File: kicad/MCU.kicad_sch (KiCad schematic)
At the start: 77 parts, among them J3 USART, J4 FAN, J5 USB_A, J6 Display, Q7 2N7002NXAK, Q8 2N7002K, Q9 2N7002K, SW1 ENC0 (Voltage), SW2 ENC1 (Current), SW3 BOOT, SW4 RST, U6 USBLC6-2SC6, U7 MCP9700A, U8 STM32F373C8Tx, Y1 Crystal

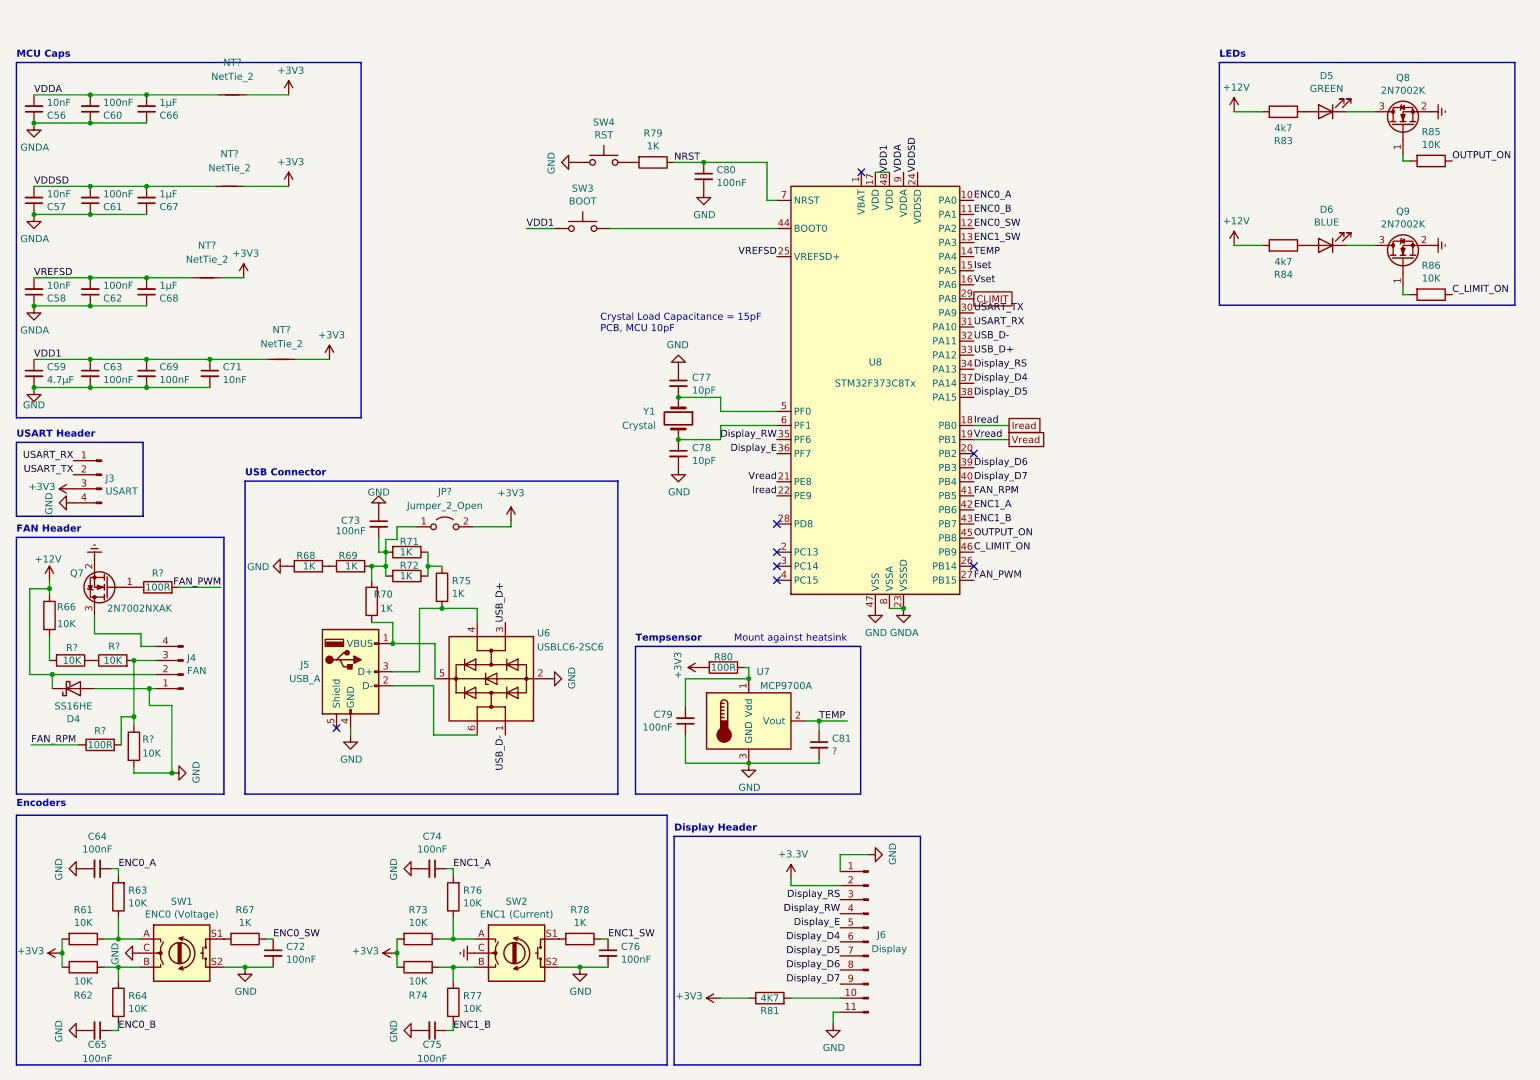
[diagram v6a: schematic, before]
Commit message: Updated files to kicad 8
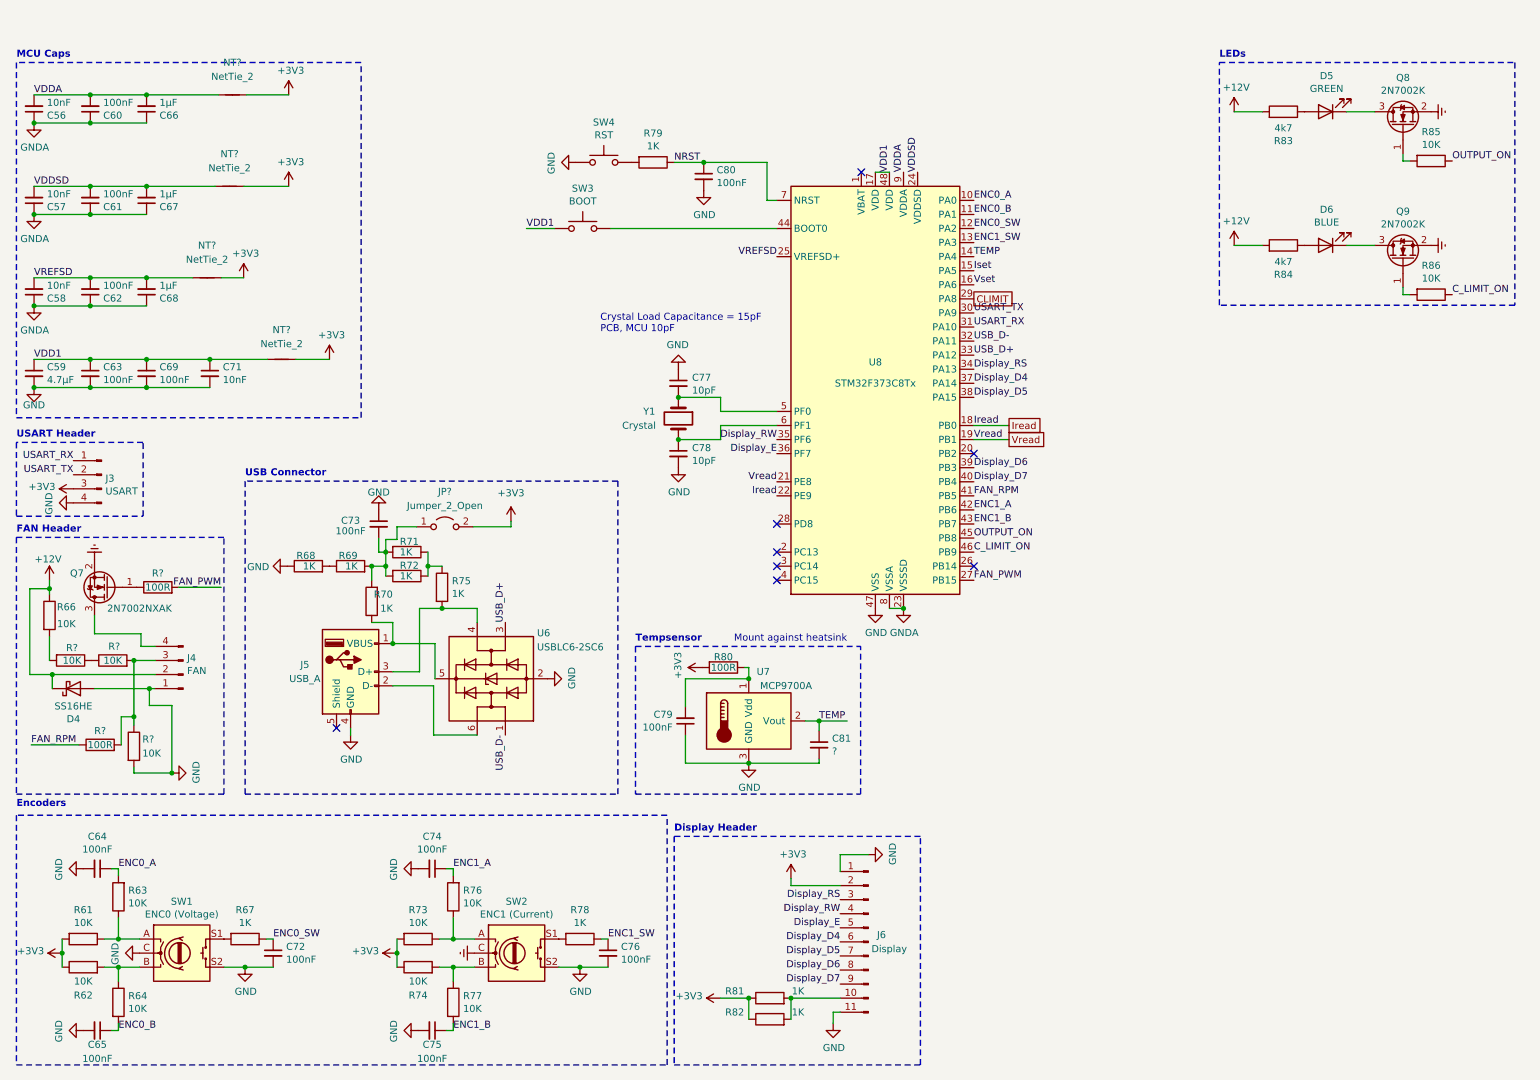
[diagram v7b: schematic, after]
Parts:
- added R82: 1K, Resistor_SMD:R_0805_2012Metric_Pad1.15x1.40mm_HandSolder, symbol Device:R
- R81: value 4K7 -> 1K
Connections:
- net +3V3: now also R82.1
- net at J6.10 (Pin_10), R81.2: now also R82.2

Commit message: Fixed a bunch of alignment
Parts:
- removed U8: STM32F373C8Tx, Package_QFP:LQFP-48_7x7mm_P0.5mm, symbol MCU_ST_STM32F3:STM32F373C8Tx
- added U6: STM32F373C8Tx, Package_QFP:LQFP-48_7x7mm_P0.5mm, symbol MCU_ST_STM32F3:STM32F373C8Tx
- J3, J4: symbol Connector:Conn_01x04_Male -> Connector:Conn_01x04_Pin
- J6: symbol Connector:Conn_01x11_Male -> Connector:Conn_01x11_Pin
- U5: renamed from U7; footprint Package_TO_SOT_THT:TO-92_Inline -> Package_TO_SOT_SMD:SOT-23; symbol Sensor_Temperature:MCP9700AT-ETT -> Sensor_Temperature:MCP9700Ax-ETT
- gave numbers to parts that had none: 10
- renumbered C56 to C18, C57 to C19, C58 to C20, C59 to C21, C60 to C22, C61 to C23, C62 to C24, C63 to C25, C64 to C26, C65 to C27, C66 to C28, C67 to C29, C68 to C30, C69 to C31, C71 to C32, C72 to C33, C73 to C34, C74 to C35, C75 to C36, C76 to C37, C77 to C38, C78 to C39, C79 to C40, C80 to C41, C81 to C42, D4 to D7, D5 to D8, D6 to D9, Q7 to Q6, Q8 to Q7, Q9 to Q8, R66 to R30, R61 to R32, R62 to R33, R63 to R36, R64 to R37, R67 to R40, R68 to R41, R69 to R42, R70 to R43, R71 to R44, R72 to R45, R73 to R46, R74 to R47, R75 to R48, R76 to R49, R77 to R50, R78 to R51, R79 to R52, R80 to R53, R81 to R54, R82 to R55, R83 to R56, R84 to R57, R85 to R58, R86 to R59, U6 to U4
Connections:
- net GNDREF is gone; now on net GND: Q6.2 (S), Q7.2 (S), Q8.2 (S), SW2.C
- net CLIMIT: now also U6.29 (PA8)
- net C_LIMIT_ON: now also U6.46 (PB9)
- net Display_D4: now also U6.37 (PA14)
- net Display_D5: now also U6.38 (PA15)
- net Display_D6: now also U6.39 (PB3)
- net Display_D7: now also U6.40 (PB4)
- net Display_E: now also U6.36 (PF7)
- net Display_RS: now also U6.34 (PA13)
- net Display_RW: now also U6.35 (PF6)
- net ENC0_A: now also U6.10 (PA0)
- net ENC0_B: now also U6.11 (PA1)
- net ENC0_SW: now also U6.12 (PA2)
- net ENC1_A: now also U6.42 (PB6)
- net ENC1_B: now also U6.43 (PB7)
- net ENC1_SW: now also U6.13 (PA3)
- net FAN_PWM: now also U6.27 (PB15)
- net FAN_RPM: now also U6.41 (PB5)
- net GND: now also U6.47 (VSS)
- net GNDA: now also U6.23 (VSSSD), U6.8 (VSSA)
- net Iread: now also U6.18 (PB0), U6.22 (PE9)
- net Iset: now also U6.15 (PA5)
- net NRST: now also U6.7 (NRST)
- net OUTPUT_ON: now also U6.45 (PB8)
- net TEMP: now also U6.14 (PA4)
- net USART_RX: now also U6.31 (PA10)
- net USART_TX: now also U6.30 (PA9)
- net USB_D+: now also U4.4 (I/O2), U6.33 (PA12); no longer U4.3 (I/O2)
- net USB_D-: now also U4.3 (I/O2), U6.32 (PA11); no longer U4.1 (I/O1)
- net VDD1: now also U6.17 (VDD), U6.48 (VDD)
- net VDDA: now also U6.9 (VDDA)
- net VDDSD: now also U6.24 (VDDSD)
- net VREFSD: now also U6.25 (VREFSD+)
- net Vread: now also U6.19 (PB1), U6.21 (PE8)
- net Vset: now also U6.16 (PA6)
- net at J5.3 (D+), R48.2: now also U4.6 (I/O1); no longer U4.4 (I/O2)
- net at J5.2 (D-): now also U4.1 (I/O1); no longer U4.6 (I/O1)
- net at SW3.1: now also U6.44 (BOOT0)
- net at C38.2, Y1.1: now also U6.5 (PF0)
- net at C39.1, Y1.2: now also U6.6 (PF1)
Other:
- moved on the sheet: C18, C20, C22, C23, C24, C26, C27, C28, C29, C30, C33, C34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
